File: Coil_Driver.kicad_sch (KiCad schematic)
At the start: 158 parts, among them J1 47346-0001, J3 NPPC122KFMS-RC, U1 SG-210STF 12.0000ML3, U10 ADP7142ARDZ-R7, U11 BUK9D23-40E, U12 BUK9D23-40E, U13 ADuM4120-1A, U14 ADuM4120-1A, U15 LT8253AJUFDM#PBF, U16 PSMNR55-40SSH, U17 PSMNR55-40SSH, U18 PSMNR55-40SSH, U19 PSMNR55-40SSH, U2 ICE40UP5K-SG48ITR, U20 BUK9D23-40E, U21 BUK9D23-40E, U22 PSMNR55-40SSH, U23 PSMNR55-40SSH, U24 PSMNR55-40SSH, U25 PSMNR55-40SSH, U26 LT3748, U27 BUK9D23-40E, U28 ADuM4120-1A, U29 ADuM4120-1A, U3 W25Q32JVSS, U4 SN74AUP2G125DCUR, U5 AP2127K-3.3, U6 LT1117CST#TRPBF, U7 AP2127K-1.2, U8 93LC56BT-I/OT, U9 FT232H

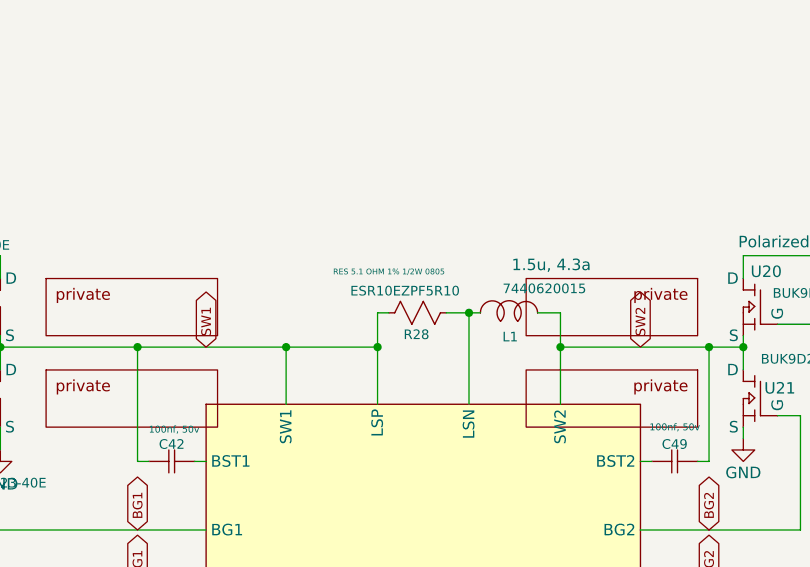
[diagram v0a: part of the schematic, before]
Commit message: Changed R28 to the correct value and part
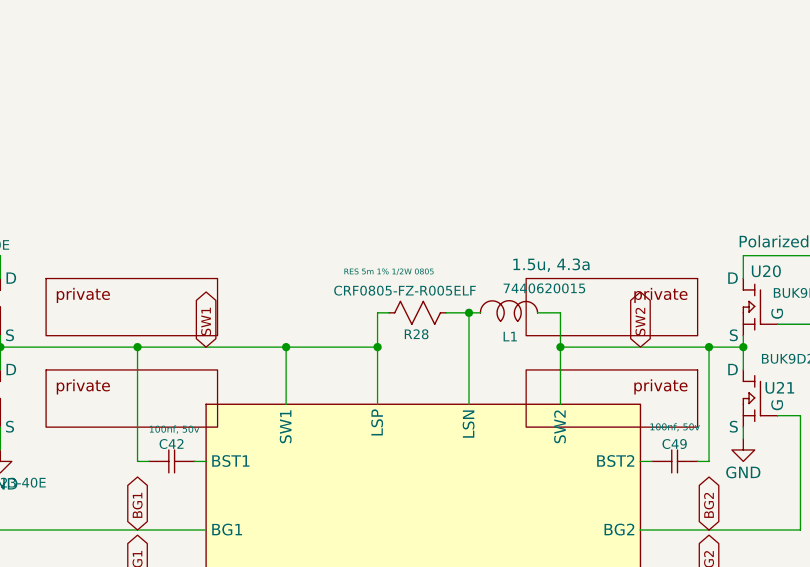
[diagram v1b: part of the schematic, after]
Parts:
- R28: value ESR10EZPF5R10 -> CRF0805-FZ-R005ELF
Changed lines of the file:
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@@
 			)
 		)
-		(property "Value" "ESR10EZPF5R10"
+		(property "Value" "CRF0805-FZ-R005ELF"
 			(at 306.578 247.142 90)
 			(effects
@@
 			)
 		)
-		(property "Datasheet" "https://fscdn.rohm.com/en/products/databook/datasheet/passive/resistor/chip_resistor/esr-e.pdf"
+		(property "Datasheet" "https://bourns.com/docs/Product-Datasheets/CRF.pdf"
 			(at 303.53 251.46 0)
 			(effects
@@
 			)
 		)
-		(property "Description" "RES 5.1 OHM 1% 1/2W 0805"
+		(property "Description" "RES 5m 1% 1/2W 0805"
 			(at 304.8 245.618 90)
 			(effects

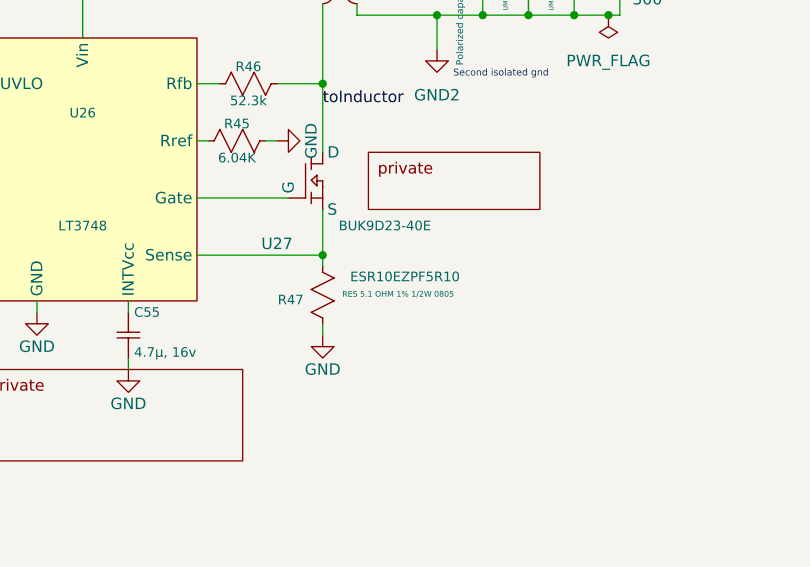
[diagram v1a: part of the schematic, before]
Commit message: Changed R47 to correct value
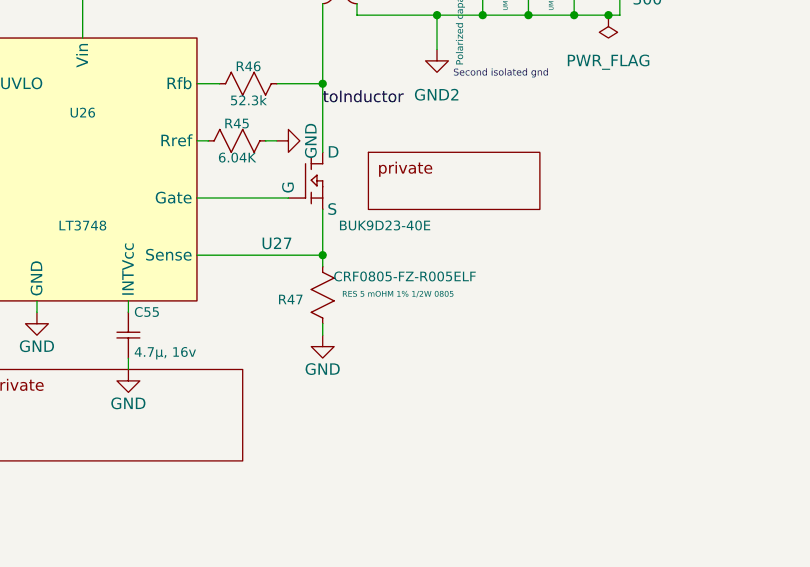
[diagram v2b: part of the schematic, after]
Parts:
- R47: value ESR10EZPF5R10 -> CRF0805-FZ-R005ELF
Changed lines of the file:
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@@
 			)
 		)
-		(property "Value" "ESR10EZPF5R10"
+		(property "Value" "CRF0805-FZ-R005ELF"
 			(at 471.424 296.418 0)
 			(effects
@@
 			)
 		)
-		(property "Datasheet" "https://fscdn.rohm.com/en/products/databook/datasheet/passive/resistor/chip_resistor/esr-e.pdf"
+		(property "Datasheet" "https://bourns.com/docs/Product-Datasheets/CRF.pdf"
 			(at 463.55 303.53 0)
 			(effects
@@
 			)
 		)
-		(property "Description" "RES 5.1 OHM 1% 1/2W 0805"
+		(property "Description" "RES 5 mOHM 1% 1/2W 0805"
 			(at 470.662 298.958 0)
 			(effects

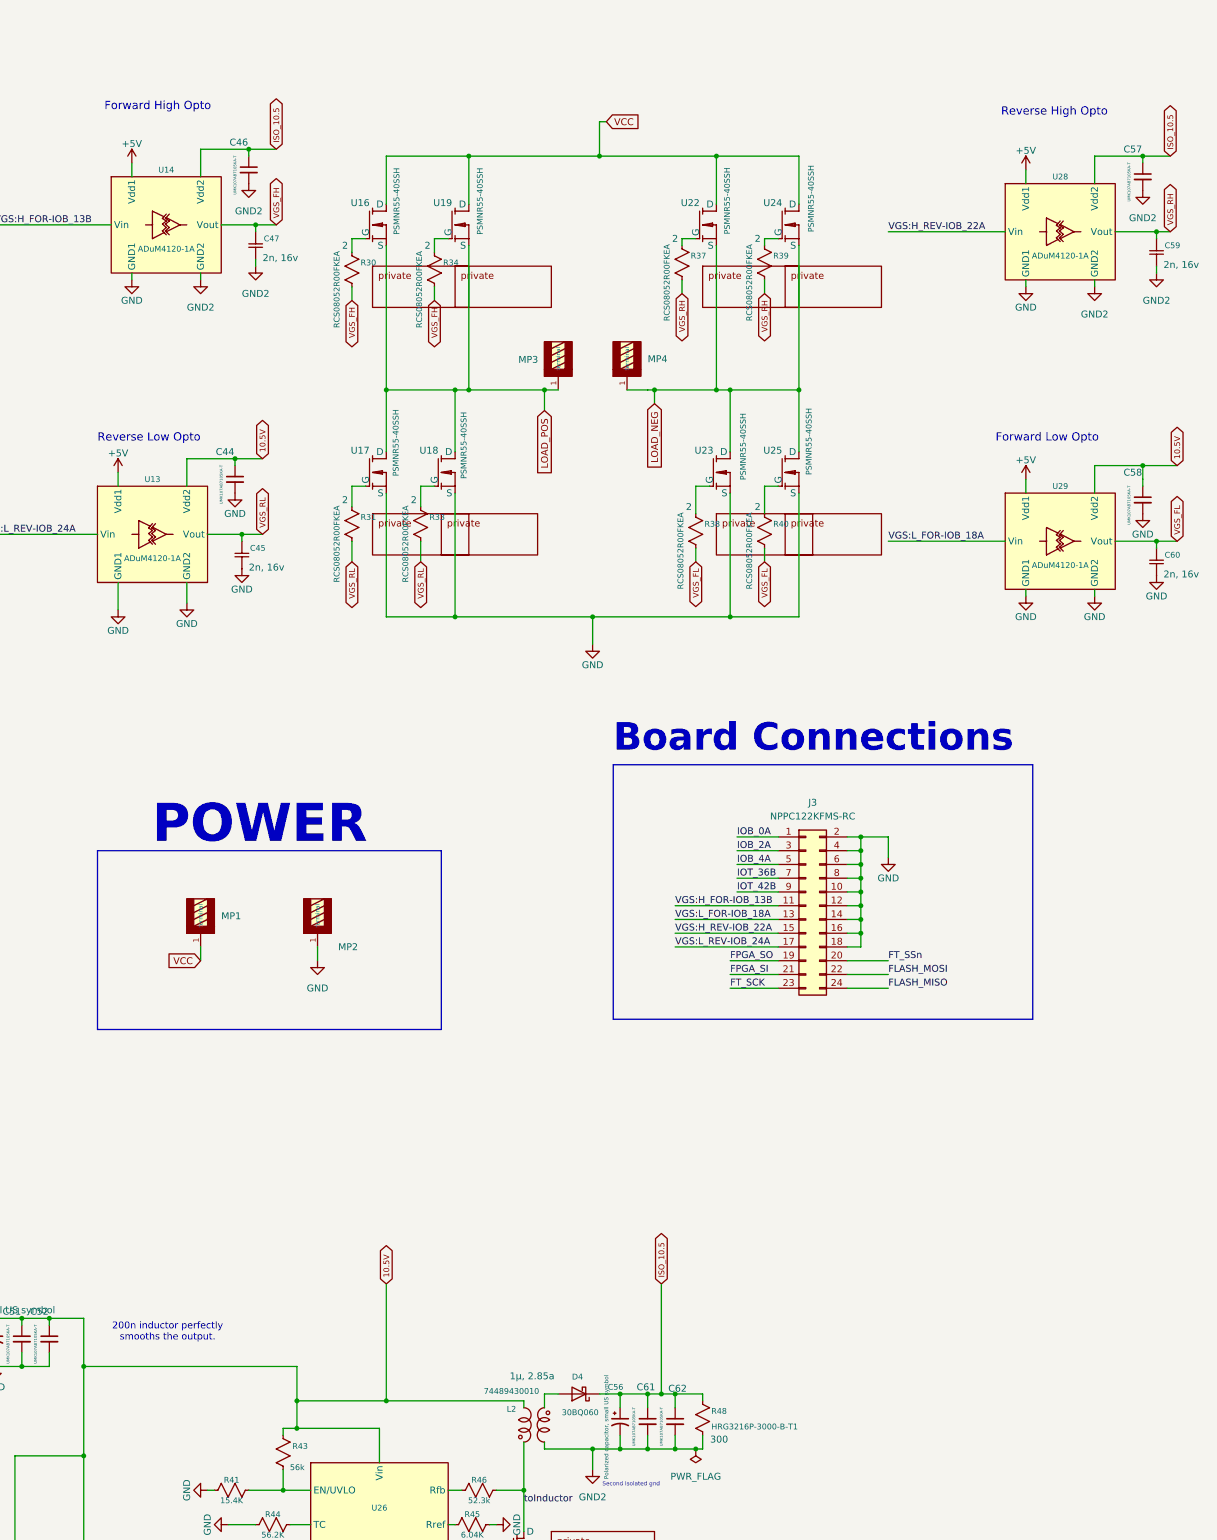
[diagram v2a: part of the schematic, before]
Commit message: Fixed L2 symbol and PCB orientation
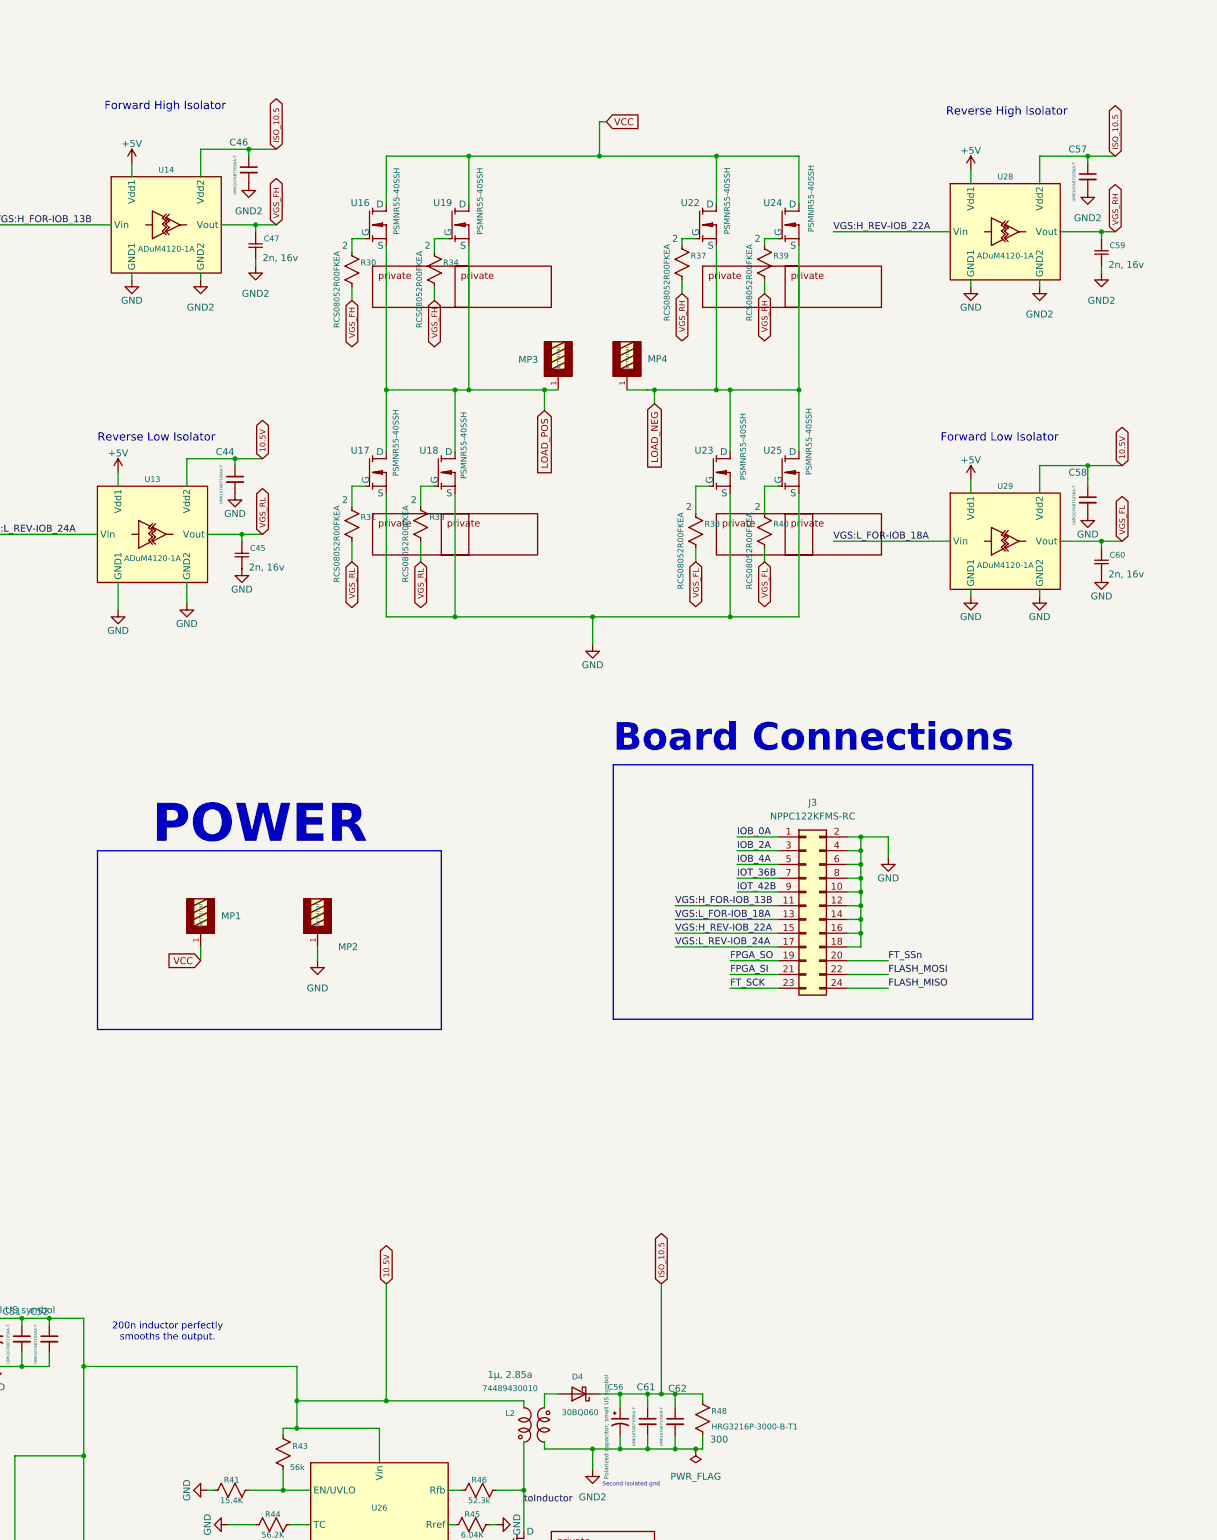
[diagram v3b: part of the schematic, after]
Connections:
- net 10.5V: now also L2.2; no longer L2.1 (A)
- net GND2: now also L2.1; no longer L2.4 (A)
- net toInductor: now also L2.3; no longer L2.2 (B)
- net at D4.2 (A): now also L2.4; no longer L2.3 (B)
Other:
- note added: "Forward High Isolator"
- note added: "Forward Low Isolator"
- note added: "Reverse High Isolator"
- note added: "Reverse Low Isolator"
- note removed: "Forward High Opto"
- note removed: "Forward Low Opto"
- note removed: "Reverse High Opto"
- note removed: "Reverse Low Opto"
- moved on the sheet: C57, C58, C59, C60, L2, U28, U29
